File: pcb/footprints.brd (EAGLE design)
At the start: 100 x 80 mm, 11 parts, among them IC1 HX711, IC2 STM32F401RET6U, IC3 LDS3985M33R, IC4 LMC555CN_NOPB, IC5 M95640-RMN6P, U1 MCP73831.SOT23-5

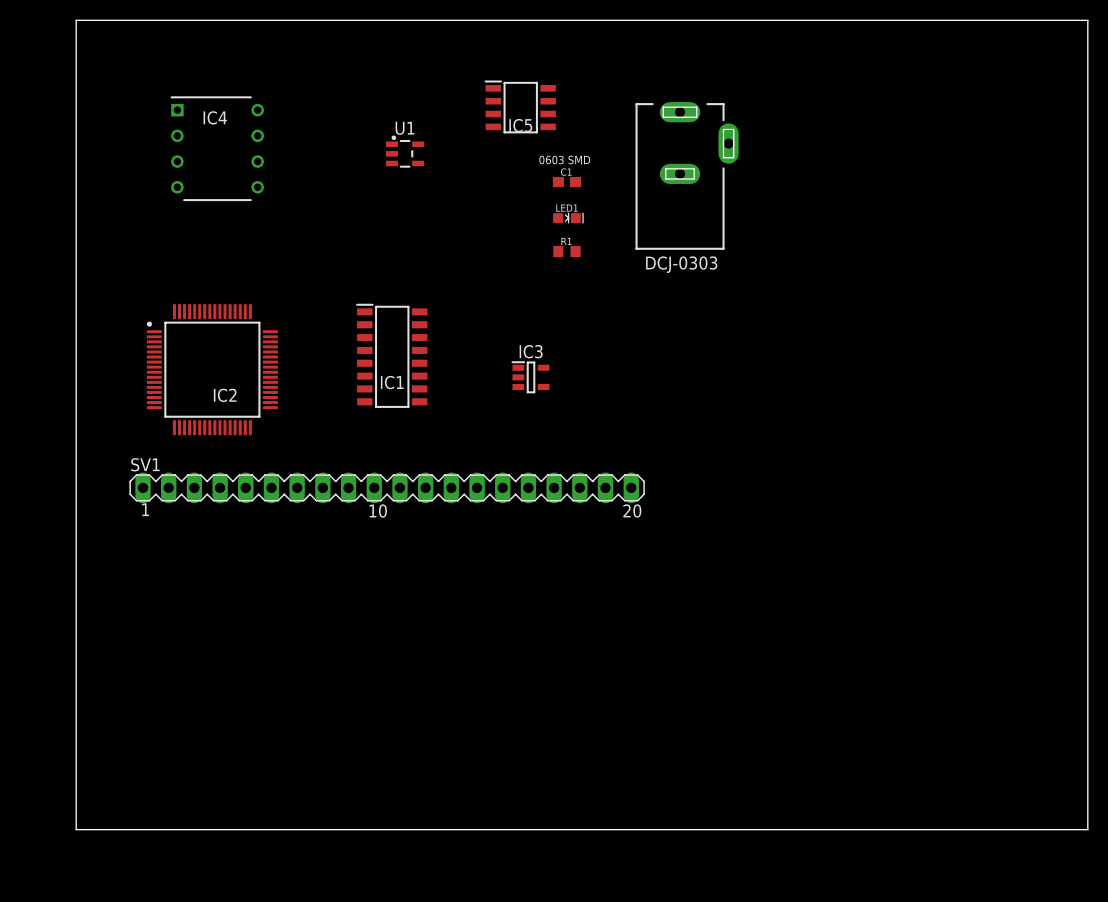
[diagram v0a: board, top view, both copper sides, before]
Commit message: Updated the PCB Schematic: 80% complete. Added PCB reference.
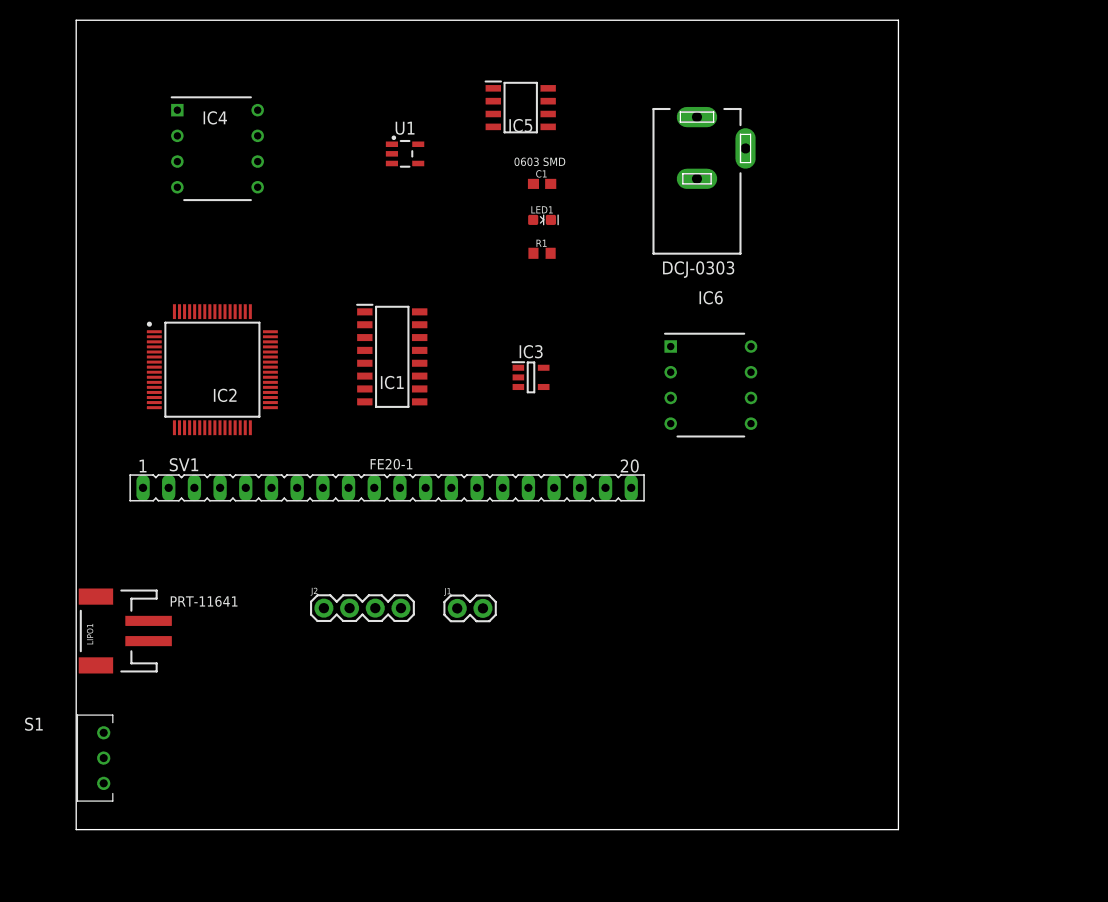
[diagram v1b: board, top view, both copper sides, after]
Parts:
- added IC6: TLV2462IP, SamacSys_Parts:DIP794W53P254L959H508Q8N
- added J1: (no value), LinnesLab-Connectors:1X02
- added J2: (no value), LinnesLab-Connectors:1X04
- added LIPO1: (no value), LinnesLab-Connectors:JST-2-SMD
- added S1: EG1270, SamacSys_Parts:EG1270
- SV1: device con-lstb:MA20-1 -> con-lsta:FE20
- moved C1 2.47 mm to (46.1, 63.8)
- moved LED1 2.47 mm to (46.1, 60.3)
- moved R1 2.47 mm to (46.1, 57.0)
- moved DCJ-0303 1.74 mm to (61.4, 67.3)
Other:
- board size 100 x 80 mm -> 81.3 x 80 mm
- board text added: "FE20-1"
- board text added: "PRT-11641"

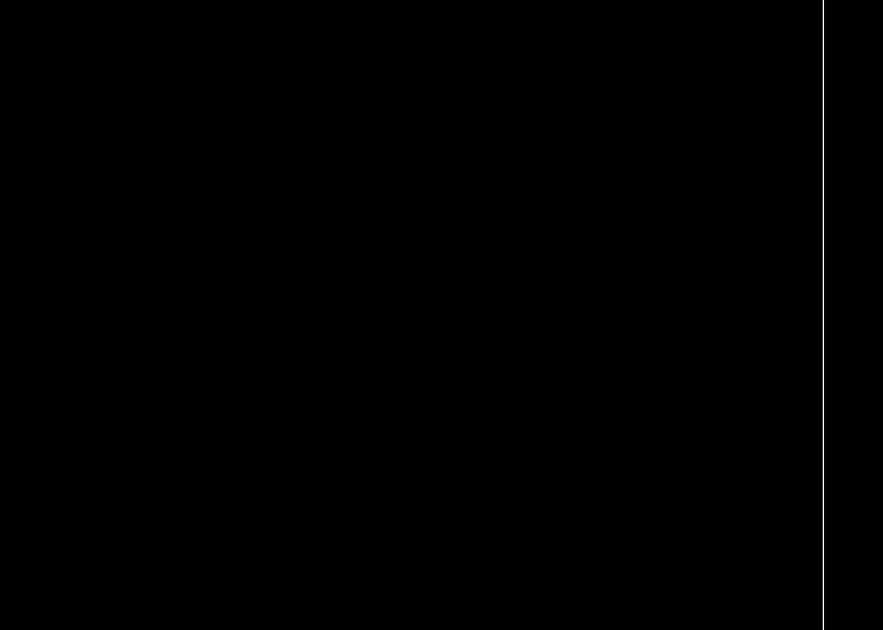
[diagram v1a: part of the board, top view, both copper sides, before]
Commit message: Added I2C EEPROM Footprint to both schematic and board and dimensioned appropriately
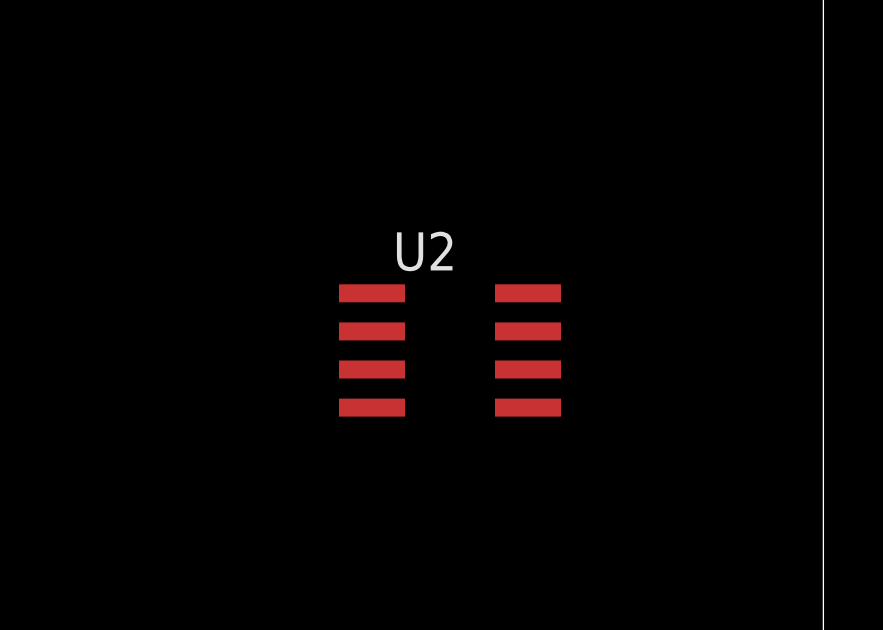
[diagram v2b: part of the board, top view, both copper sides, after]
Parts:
- added U2: BR24S64FJ-WE2, I2C-EEPROM:SOIC8
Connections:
- new net GND: U2.4
- new net VCC: U2.8
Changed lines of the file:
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@@
 <drawing>
 <settings>
-<setting alwaysvectorfont="yes"/>
+<setting alwaysvectorfont="no"/>
 <setting verticaltext="up"/>
 </settings>
-<grid distance="10" unitdist="mil" unit="mil" style="lines" multiple="1" display="yes" altdistance="1" altunitdist="mil" altunit="mil"/>
+<grid distance="1" unitdist="mil" unit="mil" style="lines" multiple="1" display="yes" altdistance="1" altunitdist="mil" altunit="mil"/>
 <layers>
 <layer number="1" name="Top" color="4" fill="1" visible="yes" active="yes"/>
@@
 <dimension x1="24.4856" y1="21.8948" x2="27.0256" y2="21.8948" x3="25.7556" y3="18.5674" textsize="1.016" layer="20" unit="mil" visible="yes"/>
 <dimension x1="37.6682" y1="21.8694" x2="40.2082" y2="21.8694" x3="38.9382" y3="17.1196" textsize="1.016" layer="20" unit="mil" visible="yes"/>
+<dimension x1="65.1256" y1="21.5138" x2="65.1256" y2="20.9042" x3="63.9064" y3="21.209" textsize="0.8128" layer="20" unit="mil" visible="yes"/>
+<dimension x1="65.1256" y1="21.5138" x2="72.517" y2="21.4884" x3="68.832109375" y3="24.64725625" textsize="0.8128" layer="20" unit="mil" visible="yes"/>
+<dimension x1="72.5424" y1="21.5138" x2="72.5424" y2="17.0942" x3="75.7936" y3="19.304" textsize="0.8128" layer="20" unit="mil" visible="yes"/>
 </plain>
 <attributes>
@@
 <attribute name="VALUE" x="1.198" y="12.8632" size="1.27" layer="27" align="center"/>
 </element>
+<element name="U2" library="I2C-EEPROM" package="SOIC8" value="BR24S64FJ-WE2" x="68.834" y="19.304" smashed="yes" rot="R270">
+<attribute name="NAME" x="66.929" y="21.971" size="1.27" layer="25"/>
+<attribute name="VALUE" x="60.0964" y="14.097" size="1.27" layer="27" rot="R358.8"/>
+</element>
 </elements>
 <signals>
@@
 <contactref element="U1" pad="2"/>
 </signal>
+<signal name="GND">
+<contactref element="U2" pad="4"/>
+</signal>
+<signal name="VCC">
+<contactref element="U2" pad="8"/>
+</signal>
 </signals>

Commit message: Updated the initial revision of the PCB + PDFs of layout
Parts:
- removed LIPO1: (no value), LinnesLab-Connectors:JST-2-SMD
- added Q1: S8550, SamacSys_Parts:MJE13001TP
- moved S1 29.1 mm to (31.8, 3.05), turned to 90 degrees
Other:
- board text removed: "PRT-11641"
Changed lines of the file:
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@@
 <setting verticaltext="up"/>
 </settings>
-<grid distance="1" unitdist="mil" unit="mil" style="lines" multiple="1" display="yes" altdistance="1" altunitdist="mil" altunit="mil"/>
+<grid distance="10" unitdist="mil" unit="mil" style="lines" multiple="1" display="yes" altdistance="1" altunitdist="mil" altunit="mil"/>
 <layers>
 <layer number="1" name="Top" color="4" fill="1" visible="yes" active="yes"/>
@@
 <dimension x1="58.7502" y1="40.1574" x2="66.7004" y2="40.1574" x3="62.7253" y3="36.4236" textsize="1.016" layer="20" unit="mil" visible="yes"/>
 <dimension x1="61.3664" y1="67.3354" x2="66.1924" y2="67.3354" x3="63.7794" y3="59.4868" textsize="1.016" layer="20" unit="mil" visible="yes"/>
-<dimension x1="9.4488" y1="20.6502" x2="9.4488" y2="18.668996875" x3="9.4488" y3="10.868996875" textsize="1.016" layer="20" dtype="radius" unit="mil" visible="yes"/>
-<text x="9.2202" y="22.0472" size="1.016" layer="25">PRT-11641</text>
 <text x="28.9814" y="35.6108" size="1.016" layer="25">FE20-1</text>
 <dimension x1="24.4856" y1="21.8948" x2="27.0256" y2="21.8948" x3="25.7556" y3="18.5674" textsize="1.016" layer="20" unit="mil" visible="yes"/>
 <dimension x1="37.6682" y1="21.8694" x2="40.2082" y2="21.8694" x3="38.9382" y3="17.1196" textsize="1.016" layer="20" unit="mil" visible="yes"/>
 <dimension x1="65.1256" y1="21.5138" x2="65.1256" y2="20.9042" x3="63.9064" y3="21.209" textsize="0.8128" layer="20" unit="mil" visible="yes"/>
-<dimension x1="65.1256" y1="21.5138" x2="72.517" y2="21.4884" x3="68.832109375" y3="24.64725625" textsize="0.8128" layer="20" unit="mil" visible="yes"/>
+<dimension x1="65.1256" y1="21.5138" x2="72.517" y2="21.4884" x3="68.831234375" y3="24.3923875" textsize="0.8128" layer="20" unit="mil" visible="yes"/>
 <dimension x1="72.5424" y1="21.5138" x2="72.5424" y2="17.0942" x3="75.7936" y3="19.304" textsize="0.8128" layer="20" unit="mil" visible="yes"/>
+<dimension x1="9.906" y1="18.034" x2="12.446" y2="18.034" x3="11.176" y3="13.716" textsize="1.778" layer="20" unit="mil" visible="yes"/>
+<dimension x1="9.906" y1="18.034" x2="9.906" y2="19.558" x3="3.302" y3="18.796" textsize="1.778" layer="20" unit="mil" visible="yes"/>
+<dimension x1="31.75" y1="3.048" x2="29.21" y2="3.048" x3="30.48" y3="7.874" textsize="1.778" layer="20" unit="mil" visible="yes"/>
 </plain>
 <attributes>
@@
 <attribute name="VALUE" x="62.738" y="50.8" size="1.27" layer="27" align="center"/>
 </element>
-<element name="LIPO1" library="LinnesLab-Connectors" package="JST-2-SMD" value="" x="3.4544" y="19.6342" smashed="yes" rot="R90">
-<attribute name="NAME" x="1.6764" y="18.2372" size="0.6096" layer="25" ratio="20" rot="R90"/>
-<attribute name="PROD_ID" value="CONN-11443" x="3.4544" y="19.6342" size="1.016" layer="27" rot="R90" display="off"/>
-<attribute name="SF_ID" value="PRT-08612" x="3.4544" y="19.6342" size="1.016" layer="27" rot="R90" display="off"/>
-<attribute name="VALUE" x="2.8194" y="17.9832" size="0.6096" layer="27" ratio="20" rot="R90"/>
-</element>
 <element name="J1" library="LinnesLab-Connectors" package="1X02" value="" x="37.6682" y="21.8694" smashed="yes">
 <attribute name="NAME" x="36.3982" y="23.2664" size="0.6096" layer="25" font="vector" ratio="20"/>
@@
 <attribute name="VALUE" x="23.2156" y="19.8628" size="0.6096" layer="27" font="vector" ratio="20"/>
 </element>
-<element name="S1" library="SamacSys_Parts" package="EG1270" value="EG1270" x="2.7178" y="4.572" smashed="yes">
-<attribute name="ARROW_PART_NUMBER" value="" x="2.7178" y="4.572" size="1.016" layer="27" display="off"/>
-<attribute name="ARROW_PRICE-STOCK" value="" x="2.7178" y="4.572" size="1.016" layer="27" display="off"/>
-<attribute name="DESCRIPTION" value="E-SWITCH - EG1270 - SWITCH, SLIDE, SPDT, 300mA, 6V, PCB" x="2.7178" y="4.572" size="1.016" layer="27" display="off"/>
-<attribute name="HEIGHT" value="4.6mm" x="2.7178" y="4.572" size="1.016" layer="27" display="off"/>
-<attribute name="MANUFACTURER_NAME" value="E-Switch" x="2.7178" y="4.572" size="1.016" layer="27" display="off"/>
-<attribute name="MANUFACTURER_PART_NUMBER" value="EG1270" x="2.7178" y="4.572" size="1.016" layer="27" display="off"/>
-<attribute name="MOUSER_PART_NUMBER" value="612-EG1270" x="2.7178" y="4.572" size="1.016" layer="27" display="off"/>
-<attribute name="MOUSER_PRICE-STOCK" value="https://www.mouser.co.uk/ProductDetail/E-Switch/EG1270?qs=xDsBkp9LkodMM2ilVTltow%3D%3D" x="2.7178" y="4.572" size="1.016" layer="27" display="off"/>
-<attribute name="NAME" x="-4.1614" y="10.4248" size="1.27" layer="25" align="center"/>
-<attribute name="VALUE" x="1.198" y="12.8632" size="1.27" layer="27" align="center"/>
+<element name="S1" library="SamacSys_Parts" package="EG1270" value="EG1270" x="31.75" y="3.048" smashed="yes" rot="R90">
+<attribute name="ARROW_PART_NUMBER" value="" x="31.75" y="3.048" size="1.016" layer="27" rot="R90" display="off"/>
+<attribute name="ARROW_PRICE-STOCK" value="" x="31.75" y="3.048" size="1.016" layer="27" rot="R90" display="off"/>
+<attribute name="DESCRIPTION" value="E-SWITCH - EG1270 - SWITCH, SLIDE, SPDT, 300mA, 6V, PCB" x="31.75" y="3.048" size="1.016" layer="27" rot="R90" display="off"/>
+<attribute name="HEIGHT" value="4.6mm" x="31.75" y="3.048" size="1.016" layer="27" rot="R90" display="off"/>
+<attribute name="MANUFACTURER_NAME" value="E-Switch" x="31.75" y="3.048" size="1.016" layer="27" rot="R90" display="off"/>
+<attribute name="MANUFACTURER_PART_NUMBER" value="EG1270" x="31.75" y="3.048" size="1.016" layer="27" rot="R90" display="off"/>
+<attribute name="MOUSER_PART_NUMBER" value="612-EG1270" x="31.75" y="3.048" size="1.016" layer="27" rot="R90" display="off"/>
+<attribute name="MOUSER_PRICE-STOCK" value="https://www.mouser.co.uk/ProductDetail/E-Switch/EG1270?qs=xDsBkp9LkodMM2ilVTltow%3D%3D" x="31.75" y="3.048" size="1.016" layer="27" rot="R90" display="off"/>
+<attribute name="NAME" x="25.8972" y="-3.8312" size="1.27" layer="25" rot="R90" align="center"/>
+<attribute name="VALUE" x="29.392" y="5.5734" size="1.27" layer="27" align="center"/>
 </element>
 <element name="U2" library="I2C-EEPROM" package="SOIC8" value="BR24S64FJ-WE2" x="68.834" y="19.304" smashed="yes" rot="R270">
@@
 <attribute name="VALUE" x="60.0964" y="14.097" size="1.27" layer="27" rot="R358.8"/>
 </element>
+<element name="Q1" library="SamacSys_Parts" package="MJE13001TP" value="S8550" x="9.906" y="18.034" smashed="yes">
+<attribute name="ARROW_PART_NUMBER" value="" x="9.906" y="18.034" size="1.778" layer="27" display="off"/>
+<attribute name="ARROW_PRICE-STOCK" value="" x="9.906" y="18.034" size="1.778" layer="27" display="off"/>
+<attribute name="DESCRIPTION" value="PNP Silicon Transistors" x="9.906" y="18.034" size="1.778" layer="27" display="off"/>
+<attribute name="HEIGHT" value="mm" x="9.906" y="18.034" size="1.778" layer="27" display="off"/>
+<attribute name="MANUFACTURER_NAME" value="MCC(Micro Commercial Components)" x="9.906" y="18.034" size="1.778" layer="27" display="off"/>
+<attribute name="MANUFACTURER_PART_NUMBER" value="S8550" x="9.906" y="18.034" size="1.778" layer="27" display="off"/>
+<attribute name="MOUSER_PART_NUMBER" value="" x="9.906" y="18.034" size="1.778" layer="27" display="off"/>
+<attribute name="MOUSER_PRICE-STOCK" value="" x="9.906" y="18.034" size="1.778" layer="27" display="off"/>
+<attribute name="NAME" x="15.6972" y="20.6226" size="1.27" layer="25" align="center"/>
+<attribute name="VALUE" x="11.303" y="22.4006" size="1.27" layer="27" align="center"/>
+</element>
 </elements>
